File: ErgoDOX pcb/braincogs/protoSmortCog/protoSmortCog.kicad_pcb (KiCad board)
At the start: 2 copper layers, 182.8 x 158.9 mm, 77 parts, among them J1 USB, J2 3.5mm, J3 JMP, J4 JMP, SW0:10 SW0:3, SW0:11 SW0:2, SW0:12 SW0:1, SW0:7 SW0:6, SW0:8 SW0:5, SW0:9 SW0:4, SW1:10 SW1:3, SW1:11 SW1:2, SW1:12 SW1:1, SW1:13 SW1:0, SW1:9 SW1:4, SW2:10 SW2:3, SW2:11 SW2:2, SW2:12 SW2:1, SW2:13 SW2:0, SW2:7 SW2:6, SW2:8 SW2:5, SW2:9 SW2:4, SW3:10 SW3:3, SW3:11 SW3:2, SW3:12 SW3:1, SW3:13 SW3:0, SW3:8 SW3:5, SW3:9 SW3:4, SW4:10 SW4:3, SW4:11 SW4:2, SW4:12 SW4:1, SW4:13 SW4:0, SW4:7 SW4:6, SW4:8 SW4:5, SW4:9 SW4:4, SW5:10 SW5:3, SW5:11 SW5:2, SW5:12 SW5:1, SW5:13 SW5:0, SW5:7 SW5:6, SW5:8 SW5:5, SW5:9 SW5:4, U1 TEENSY2.0, U2 MCP23018

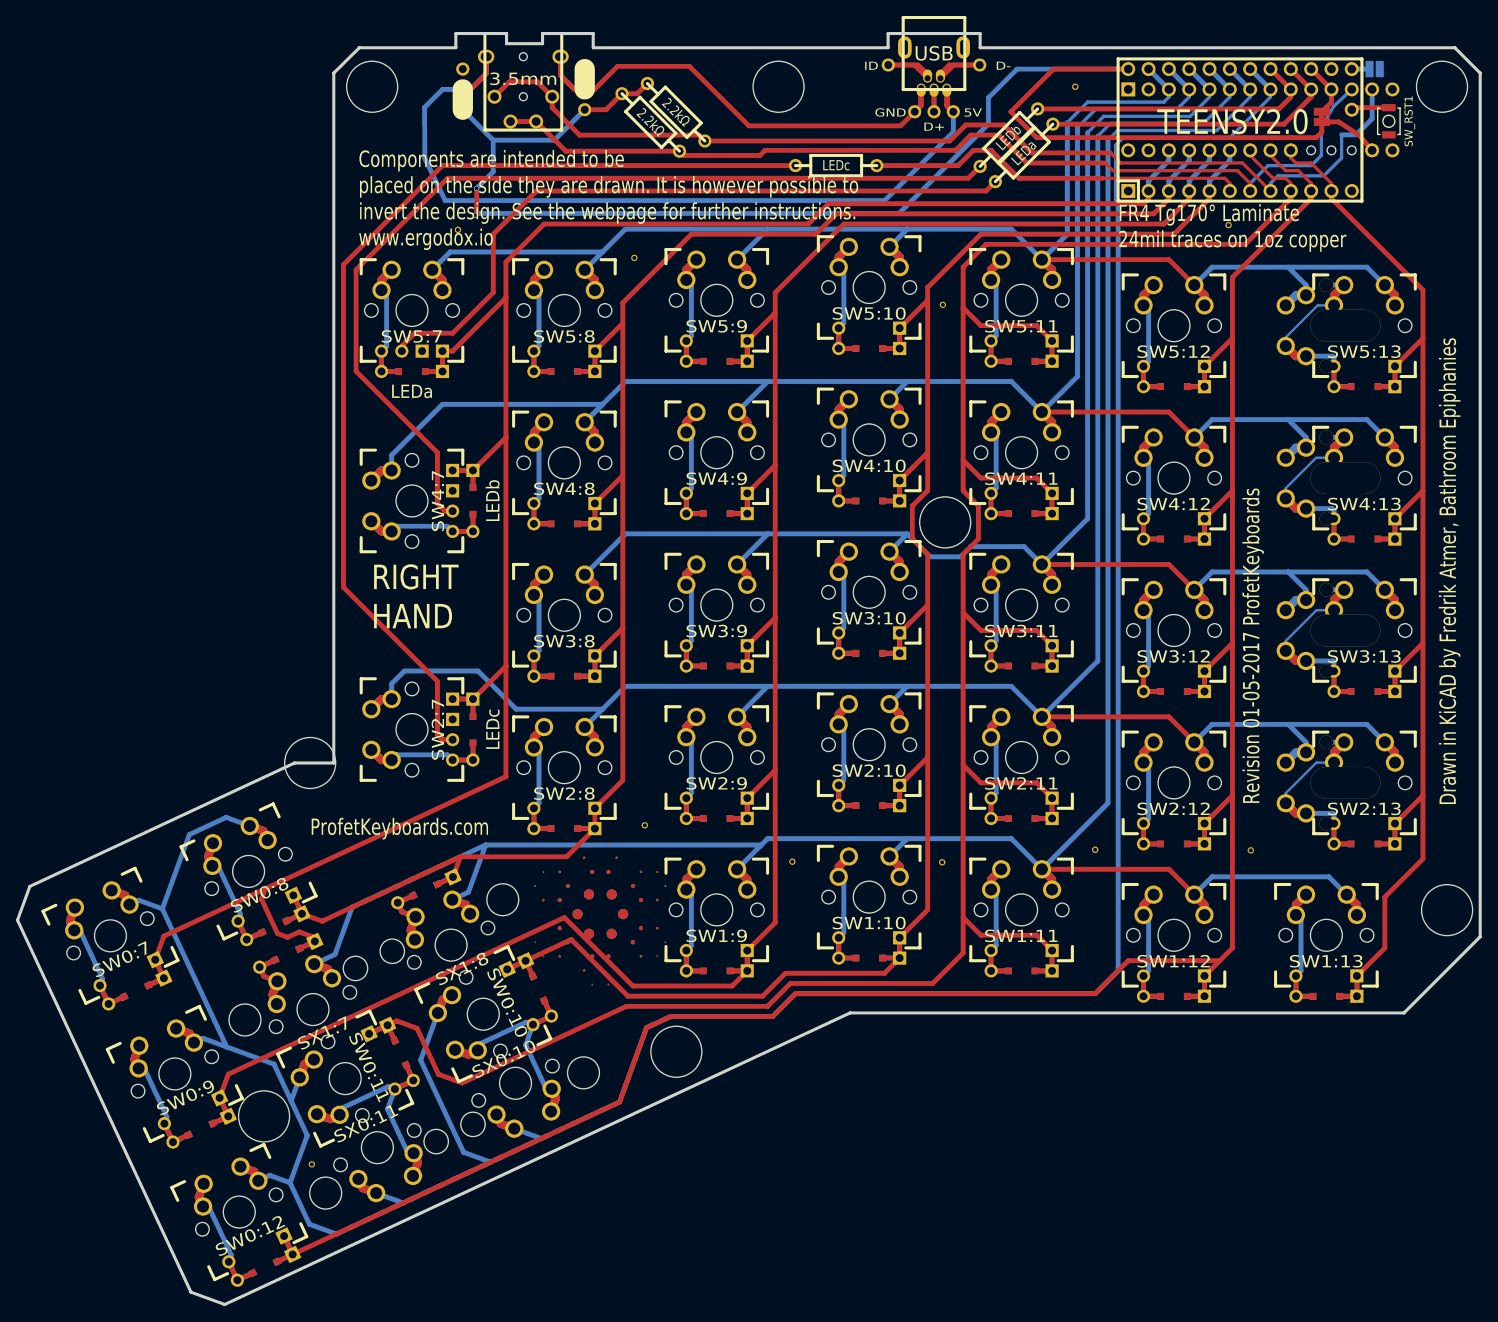
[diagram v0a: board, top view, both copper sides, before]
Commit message: adjusting former ergodox project for a smart cog template (WIP)
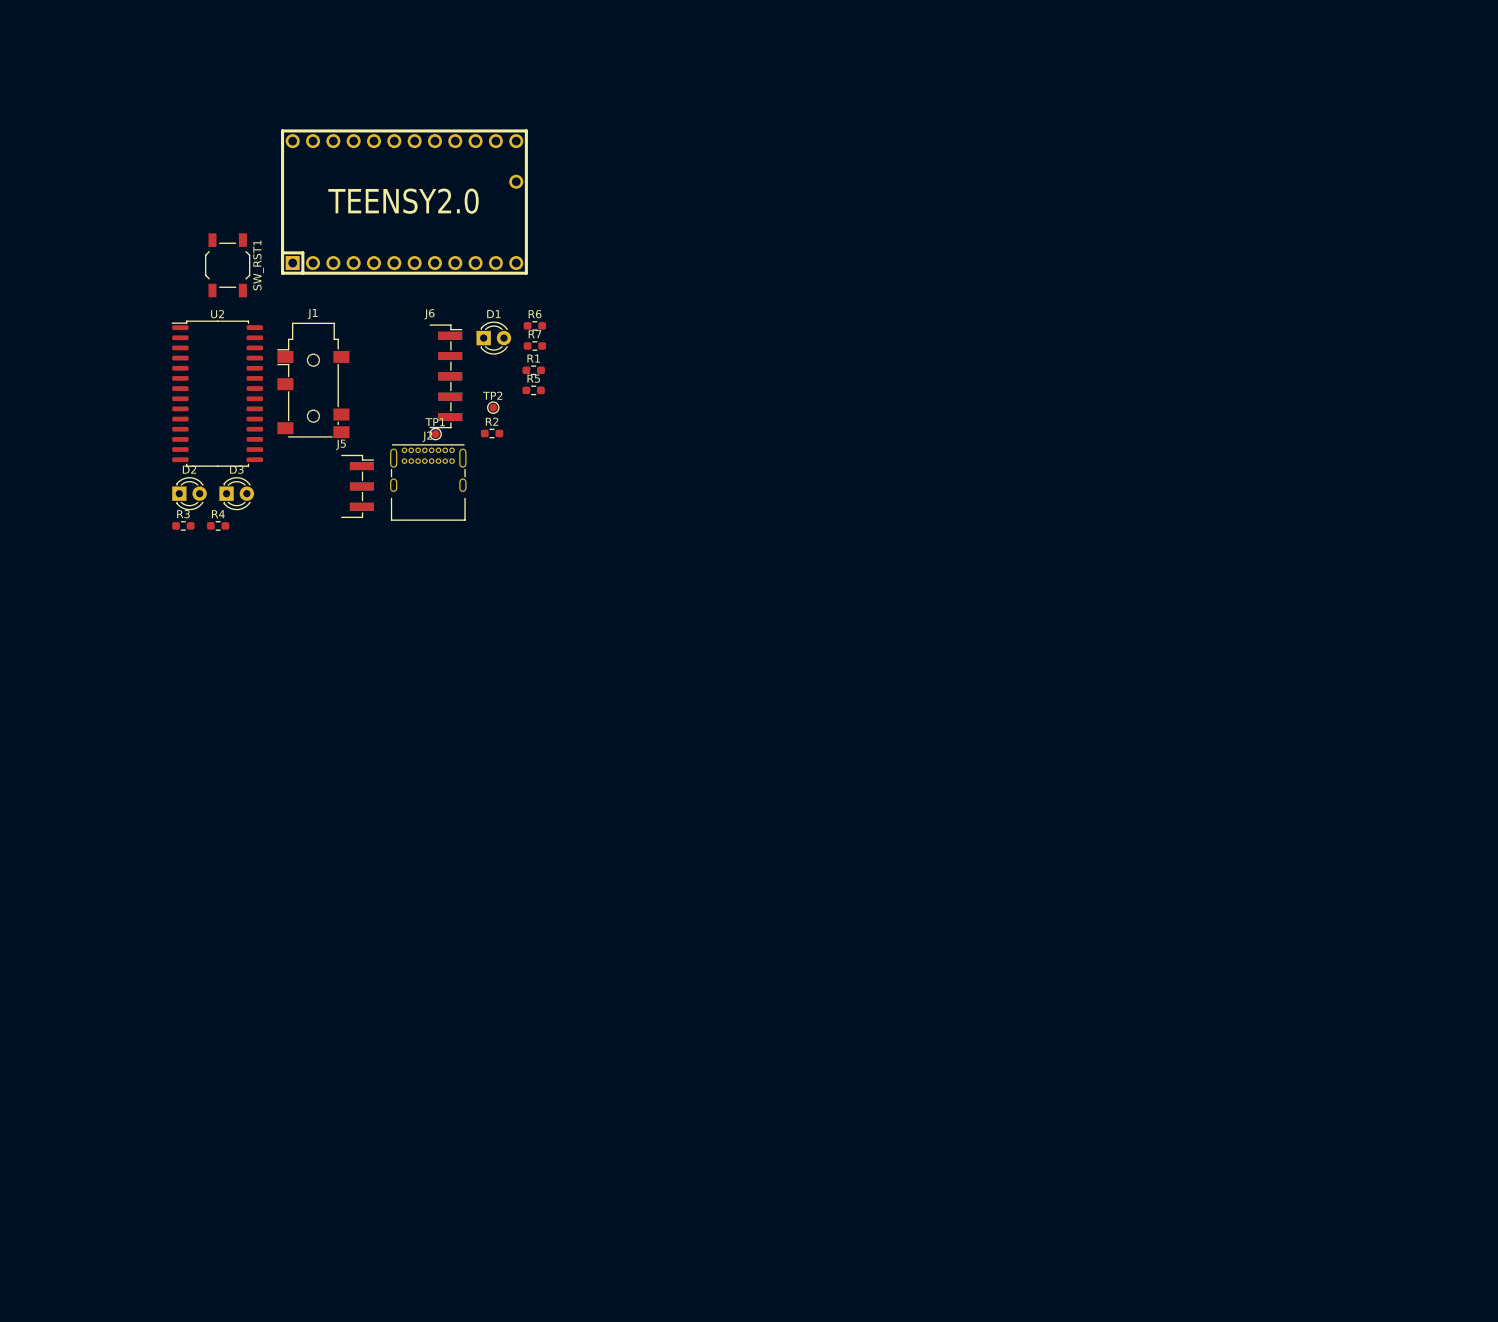
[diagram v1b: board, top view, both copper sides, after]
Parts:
- removed D1:7, D1:8: D, DIODE
- removed H99: MECHANICAL, ErgoDOXmech
- removed J3, J4: JMP, 100PITCH1X3
- removed JP1, JP2: JUMPER, GAP
- removed LED_A1: LEDa, MX_LED
- removed LED_B1: LEDb, MX_LED
- removed LED_C1: LEDc, MX_LED
- removed RA1: LEDa, RESISTOR
- removed RB1: LEDb, RESISTOR
- removed RC1: LEDc, RESISTOR
- removed S1, S2: STAB200, STAB_PCB940
- removed STAR_1: STAR_FRONT, ErgoDOX pcb:STAR
- removed STAR_2: STAR_BACK, ErgoDOX pcb:STAR
- removed STITCHING_VIA (x11): ~, lib_footprints:STITCHING_VIA
- removed SW0:10: SW0:3, ErgoDOX pcb:MX_FLIP_DIODE
- removed SW0:11: SW0:2, ErgoDOX pcb:MX_FLIP_DIODE
- removed SW0:12: SW0:1, ErgoDOX pcb:MX_FLIP_DIODE
- removed SW0:7: SW0:6, ErgoDOX pcb:MX_FLIP_DIODE
- removed SW0:8: SW0:5, ErgoDOX pcb:MX_FLIP_DIODE
- removed SW0:9: SW0:4, ErgoDOX pcb:MX_FLIP_DIODE
- removed SW1:10: SW1:3, ErgoDOX pcb:MX_FLIP_DIODE
- removed SW1:11: SW1:2, ErgoDOX pcb:MX_FLIP_DIODE
- removed SW1:12: SW1:1, ErgoDOX pcb:MX_FLIP_DIODE
- removed SW1:13: SW1:0, ErgoDOX pcb:MX_FLIP_DIODE
- removed SW1:9: SW1:4, ErgoDOX pcb:MX_FLIP_DIODE
- removed SW2:10: SW2:3, ErgoDOX pcb:MX_FLIP_DIODE
- removed SW2:11: SW2:2, ErgoDOX pcb:MX_FLIP_DIODE
- removed SW2:12: SW2:1, ErgoDOX pcb:MX_FLIP_DIODE
- removed SW2:13: SW2:0, ErgoDOX pcb:MX_FLIP_XX
- removed SW2:7: SW2:6, ErgoDOX pcb:MX_FLIP_DIODE
- removed SW2:8: SW2:5, ErgoDOX pcb:MX_FLIP_DIODE
- removed SW2:9: SW2:4, ErgoDOX pcb:MX_FLIP_DIODE
- removed SW3:10: SW3:3, ErgoDOX pcb:MX_FLIP_DIODE
- removed SW3:11: SW3:2, ErgoDOX pcb:MX_FLIP_DIODE
- removed SW3:12: SW3:1, ErgoDOX pcb:MX_FLIP_DIODE
- removed SW3:13: SW3:0, ErgoDOX pcb:MX_FLIP_XX
- removed SW3:8: SW3:5, ErgoDOX pcb:MX_FLIP_DIODE
- removed SW3:9: SW3:4, ErgoDOX pcb:MX_FLIP_DIODE
- removed SW4:10: SW4:3, ErgoDOX pcb:MX_FLIP_DIODE
- removed SW4:11: SW4:2, ErgoDOX pcb:MX_FLIP_DIODE
- removed SW4:12: SW4:1, ErgoDOX pcb:MX_FLIP_DIODE
- removed SW4:13: SW4:0, ErgoDOX pcb:MX_FLIP_XX
- removed SW4:7: SW4:6, ErgoDOX pcb:MX_FLIP_DIODE
- removed SW4:8: SW4:5, ErgoDOX pcb:MX_FLIP_DIODE
- removed SW4:9: SW4:4, ErgoDOX pcb:MX_FLIP_DIODE
- removed SW5:10: SW5:3, ErgoDOX pcb:MX_FLIP_DIODE
- removed SW5:11: SW5:2, ErgoDOX pcb:MX_FLIP_DIODE
- removed SW5:12: SW5:1, ErgoDOX pcb:MX_FLIP_DIODE
- removed SW5:13: SW5:0, ErgoDOX pcb:MX_FLIP_XX
- removed SW5:7: SW5:6, ErgoDOX pcb:MX_FLIP_DIODE
- removed SW5:8: SW5:5, ErgoDOX pcb:MX_FLIP_DIODE
- removed SW5:9: SW5:4, ErgoDOX pcb:MX_FLIP_DIODE
- removed SX0:10: SX0:3, MX_FLIP
- removed SX0:11: SX0:2, MX_FLIP
- removed SX1:7: SX1:6, MX_FLIP
- removed SX1:8: SX1:5, MX_FLIP
- added D1: LED, LED_THT:LED_D3.0mm_Clear, F.Cu at (81.3, 68.5)
- added D2: LED, LED_THT:LED_D3.0mm_Clear, F.Cu at (43.3, 88.0)
- added D3: LED, LED_THT:LED_D3.0mm_Clear, F.Cu at (49.2, 88.0)
- added J5: Conn_01x06, ergodox:ErgoCogs_sidecon_top, F.Cu at (66.2, 84.5)
- added J6: Conn_01x10, ergodox:ErgoCogs_sidecon_bot, F.Cu at (77.2, 68.2)
- added R3: 4k7, Resistor_SMD:R_0603_1608Metric_Pad0.98x0.95mm_HandSolder, F.Cu at (43.8, 92.0)
- added R4: 4k7, Resistor_SMD:R_0603_1608Metric_Pad0.98x0.95mm_HandSolder, F.Cu at (48.2, 92.0)
- added R5: 4k7, Resistor_SMD:R_0603_1608Metric_Pad0.98x0.95mm_HandSolder, F.Cu at (87.6, 75.1)
- added R6: 4k7, Resistor_SMD:R_0603_1608Metric_Pad0.98x0.95mm_HandSolder, F.Cu at (87.8, 67.0)
- added R7: 4k7, Resistor_SMD:R_0603_1608Metric_Pad0.98x0.95mm_HandSolder, F.Cu at (87.8, 69.5)
- added TP1: TestPoint_Small, TestPoint:TestPoint_Pad_D1.0mm, F.Cu at (75.3, 80.5)
- added TP2: TestPoint_Small, TestPoint:TestPoint_Pad_D1.0mm, F.Cu at (82.5, 77.2)
- J1: value USB -> AudioJack4_SwitchTR1; footprint USBMINImod -> Connector_Audio:Jack_3.5mm_PJ311_Horizontal
- J2: value 3.5mm -> USB_C_Receptacle_USB2.0; footprint 4pin35mmAudio -> Connector_USB:USB_C_Receptacle_GCT_USB4085
- R1, R2: value 2.2kΩ -> 4k7; footprint RESISTOR -> Resistor_SMD:R_0603_1608Metric_Pad0.98x0.95mm_HandSolder
- SW_RST1: footprint Buttons_Switches_SMD:SW_SPST_B3U-1000P -> Button_Switch_SMD:SW_SPST_TL3342
- U1: footprint ErgoDOX pcb:TEENSY_2.0_WITH_RESET -> ergodox:TEENSY_2.0_WITH_RESET
- U2: value MCP23018 -> MCP23017_SO; footprint DIP28_300 -> Package_SO:SOIC-28W_7.5x17.9mm_P1.27mm; moved to F.Cu
- moved SW_RST1 146.3 mm to (49.4, 59.5)
- moved U2 134.8 mm to (48.1, 75.5)
- moved U1 104.8 mm to (71.5, 51.5)
- moved J1 89.7 mm to (60.1, 75.6), turned to 0 degrees
- moved J2 54.2 mm to (71.5, 82.6), turned to 0 degrees
- moved R2 43.7 mm to (82.4, 80.5), turned to 0 degrees
- moved R1 36.8 mm to (87.6, 72.6), turned to 0 degrees
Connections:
- J1 pad 1: Net-(J1-Pad1) -> (no net)
- J1 pad 2: Net-(J1-Pad2) -> (no net)
- J1 pad 3: Net-(J1-Pad3) -> (no net)
- J1 pad 4: Net-(J1-Pad4) -> (no net)
- J1 pad 5: Net-(J1-Pad5) -> (no net)
- J1 pad 6: GND -> (no net)
- R1 pad 1: VCC -> /LED_A
- R1 pad 2: /SDAM -> Net-(D1-Pad2)
- R2 pad 1: VCC -> /LED_B
- R2 pad 2: /SCLM -> Net-(D2-Pad2)
- U1 pad 10: /COL1 -> (no net)
- U1 pad 11: /COL0 -> (no net)
- U1 pad 12: Net-(U1-Pad12) -> (no net)
- U1 pad 19: Net-(U1-Pad19) -> (no net)
- U1 pad 2: /COL6 -> (no net)
- U1 pad 3: /COL5 -> (no net)
- U1 pad 4: /COL4 -> (no net)
- U1 pad 5: /COL10 -> (no net)
- U1 pad 7: /SCLM -> /SCL
- U1 pad 8: /SDAM -> /SDA
- U1 pad 9: /COL11 -> (no net)
- U2 pad 1: GND -> /ROW5
- U2 pad 10: /LED_A -> GND
- U2 pad 11: VCC -> (no net)
- U2 pad 12: /SCLM -> /SCL
- U2 pad 13: /SDAM -> /SCL
- U2 pad 14: Net-(U2-Pad14) -> (no net)
- U2 pad 15: GND -> (no net)
- U2 pad 16: VCC -> (no net)
- U2 pad 17: Net-(U2-Pad17) -> (no net)
- U2 pad 18: Net-(U2-Pad18) -> VCC
- U2 pad 19: Net-(U2-Pad19) -> (no net)
- U2 pad 2: (no net) -> /ROW4
- U2 pad 20: /COL0 -> (no net)
- U2 pad 21: /COL1 -> /COL0
- U2 pad 22: /COL11 -> /COL1
- U2 pad 23: /COL10 -> /COL2
- U2 pad 24: /COL4 -> /COL3
- U2 pad 25: /COL5 -> /COL4
- U2 pad 26: /COL6 -> /COL5
- U2 pad 27: Net-(U2-Pad27) -> /COL6
- U2 pad 28: Net-(U2-Pad28) -> (no net)
- U2 pad 3: /ROW5 -> /ROW3
- U2 pad 4: /ROW4 -> /ROW2
- U2 pad 5: /ROW3 -> /ROW1
- U2 pad 6: /ROW2 -> /ROW0
- U2 pad 7: /ROW1 -> /LED_B
- U2 pad 8: /ROW0 -> /LED_A
- U2 pad 9: /LED_B -> (no net)
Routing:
- net /ROW0: track 404.2 -> 0.00 mm
- net /ROW1: track 318.2 -> 0.00 mm
- net /COL11: track 316.5 -> 0.00 mm
- net /ROW2: track 295.3 -> 0.00 mm
- net /COL1: track 291.8 -> 0.00 mm
- net /COL4: track 274.3 -> 0.00 mm
- net /COL6: track 259.5 -> 0.00 mm
- net /ROW4: track 257.4 -> 0.00 mm
- net /ROW3: track 238.7 -> 0.00 mm
- net /COL10: track 233.7 -> 0.00 mm
- net /COL5: track 225.8 -> 0.00 mm
- net /ROW5: track 225.1 -> 0.00 mm
- net VCC: track 204.8 -> 0.00 mm, vias 2 -> 0
- net /COL0: track 159.7 -> 0.00 mm
- net /SDAM: track 128.3 -> 0.00 mm
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- removed copper zone on B.Cu, net GND
- removed copper zone on F.Cu, net GND
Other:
- board outline removed
- board text removed: "5V"
- board text removed: "Components are intended to be placed on the side they are drawn. It is however possible to invert the design. See the webpage for further instructions. www.ergodox.io"
- board text removed: "D+"
- board text removed: "D-"
- board text removed: "Drawn in KiCAD by Fredrik Atmer, Bathroom Epiphanies"
- board text removed: "GND"
- board text removed: "ID"
- board text removed: "RIGHT HAND"
- board text removed: "Revision 01-05-2017 ProfetKeyboards"

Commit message: 1st version of braincogs
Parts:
- removed D3: LED, LED_THT:LED_D3.0mm_Clear
- removed R3: 4k7, Resistor_SMD:R_0603_1608Metric_Pad0.98x0.95mm_HandSolder
- removed TP1, TP2: TestPoint_Small, TestPoint:TestPoint_Pad_D1.0mm
- J1: value AudioJack4_SwitchTR1 -> AudioJack4; footprint Connector_Audio:Jack_3.5mm_PJ311_Horizontal -> ergodox:CLIFF_FC68125
- J5: footprint ergodox:ErgoCogs_sidecon_top -> ergodox:ErgoCogs_sidecon_brain_top
- J6: footprint ergodox:ErgoCogs_sidecon_bot -> ergodox:ErgoCogs_sidecon_brain_bot
- U2: value MCP23017_SO -> MCP23018; footprint Package_SO:SOIC-28W_7.5x17.9mm_P1.27mm -> Package_DIP:DIP-28_W7.62mm; moved to B.Cu
- moved D2 96.0 mm to (137.5, 69.2), turned to 270 degrees
- moved U2 90.7 mm to (138.7, 78.3), turned to 180 degrees
- moved J5 83.9 mm to (148.5, 68.7)
- moved R4 83.7 mm to (128.4, 115.8)
- moved J2 83.3 mm to (148.0, 49.9), turned to 180 degrees
- moved SW_RST1 82.6 mm to (131.5, 68.2)
- moved J1 77.5 mm to (134.1, 52.6), turned to 180 degrees
- moved J6 75.1 mm to (148.2, 92.5)
- moved U1 73.9 mm to (135.0, 89.2), turned to 270 degrees
- moved R1 60.8 mm to (146.6, 87.4)
- moved R5 60.8 mm to (146.6, 89.9)
- moved R6 60.8 mm to (146.8, 81.8)
- moved R7 60.8 mm to (146.8, 84.3)
- moved R2 58.8 mm to (140.9, 86.0)
- moved D1 58.4 mm to (138.5, 80.8)
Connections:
- J5 pad 1: /ROW5 -> /ROW0
- J5 pad 2: /ROW4 -> /ROW1
- J5 pad 3: /ROW3 -> /ROW2
- J5 pad 4: /ROW2 -> /ROW3
- J5 pad 5: /ROW1 -> /ROW4
- J5 pad 6: /ROW0 -> /ROW5
- J6 pad 10: /COL0 -> /COL0_13
- J6 pad 2: (no net) -> /LED_GPIO
- J6 pad 4: /COL6 -> /COL6_7
- J6 pad 5: /COL5 -> /COL5_8
- J6 pad 6: /COL4 -> /COL4_9
- J6 pad 7: /COL3 -> /COL3_10
- J6 pad 8: /COL2 -> /COL2_11
- J6 pad 9: /COL1 -> /COL1_12
- U1 pad 6: /LED_C -> /LED_GPIO
- U2 pad 1: /ROW5 -> GND
- U2 pad 10: GND -> /LED_A
- U2 pad 11: (no net) -> VCC
- U2 pad 13: /SCL -> /SDA
- U2 pad 15: (no net) -> GND
- U2 pad 16: (no net) -> VCC
- U2 pad 18: VCC -> (no net)
- U2 pad 2: /ROW4 -> (no net)
- U2 pad 20: (no net) -> /COL0_13
- U2 pad 21: /COL0 -> /COL1_12
- U2 pad 22: /COL1 -> /COL2_11
- U2 pad 23: /COL2 -> /COL3_10
- U2 pad 24: /COL3 -> /COL4_9
- U2 pad 25: /COL4 -> /COL5_8
- U2 pad 26: /COL5 -> /COL6_7
- U2 pad 27: /COL6 -> (no net)
- U2 pad 3: /ROW3 -> /ROW5
- U2 pad 4: /ROW2 -> /ROW4
- U2 pad 5: /ROW1 -> /ROW3
- U2 pad 6: /ROW0 -> /ROW2
- U2 pad 7: /LED_B -> /ROW1
- U2 pad 8: /LED_A -> /ROW0
- U2 pad 9: (no net) -> /LED_B
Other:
- board outline added: 37 x 86 mm
- board text removed: "Design by Dominic Beauchamp, based on the Key64 by Nestor A. Diaz"
- board text removed: "ErgoDox"
- board text removed: "FR4 Tg170° Laminate 24mil traces on 1oz copper"
- board text removed: "LEFT HAND"
- board text removed: "ProfetKeyboards.com"
